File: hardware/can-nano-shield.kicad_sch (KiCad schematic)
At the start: 21 parts, among them J1 Conn_01x15_Socket, J2 Conn_01x15_Socket, J3 Conn_01x04_Pin, J4 Screw_Terminal_01x03, U1 MCP2515-xSO, U2 TJA1051T-3, Y2 16MHz 9pF

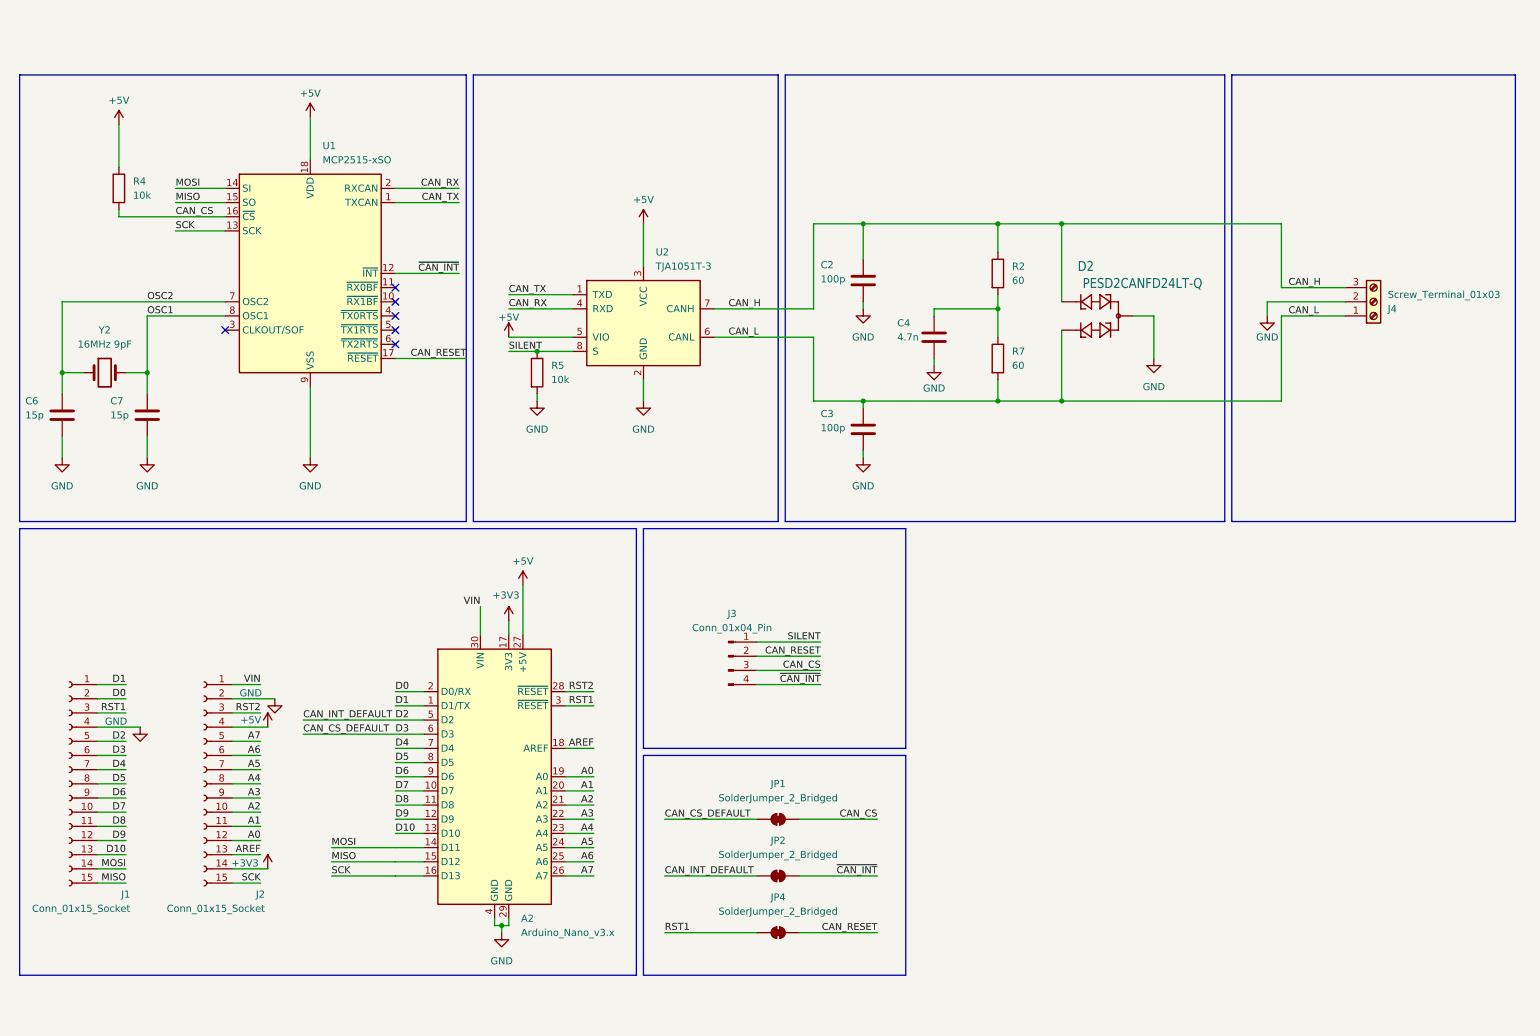
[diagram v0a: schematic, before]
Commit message: added image with cmc revision
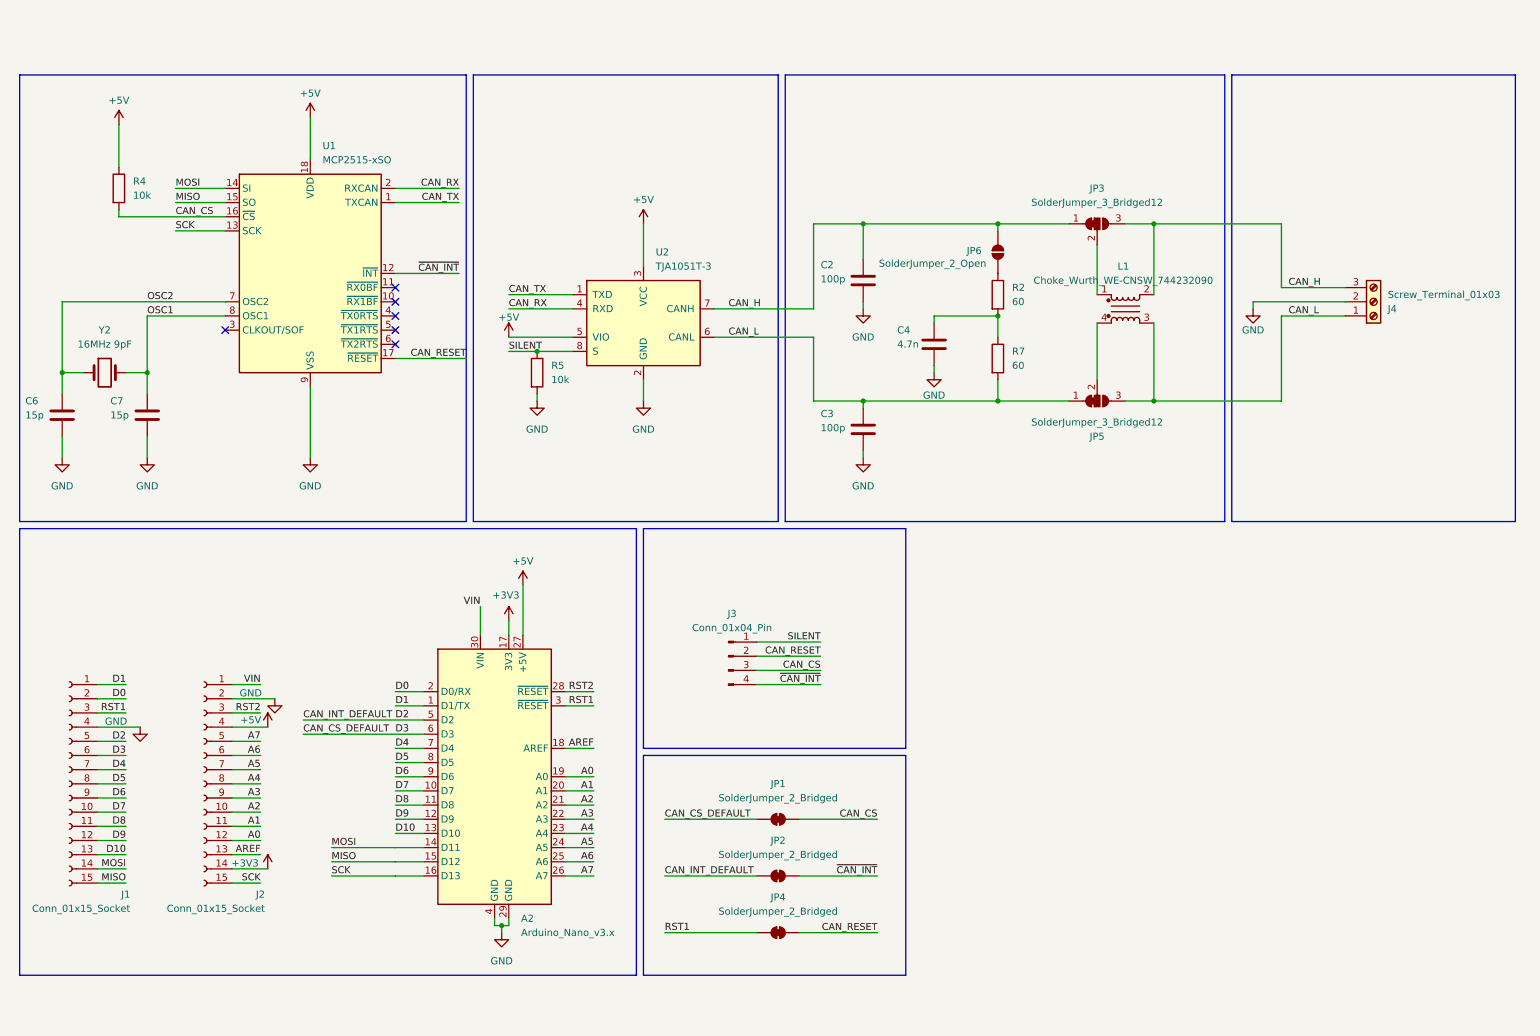
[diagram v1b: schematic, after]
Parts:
- removed D2: PESD2CANFD24LT-Q, Package_TO_SOT_SMD:TSOT-23, symbol kml-custom:PESD2CANFD24LT-Q
- added JP3, JP5: SolderJumper_3_Bridged12, symbol Jumper:SolderJumper_3_Bridged12
- added JP6: SolderJumper_2_Open, symbol Jumper:SolderJumper_2_Open
- added L1: Choke_Wurth_WE-CNSW_744232090, Inductor_SMD:L_CommonMode_Wurth_WE-CNSW-1206, symbol Filter:Choke_Wurth_WE-CNSW_744232090
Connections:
- net CAN_H: now also JP3.1 (A), JP3.3 (B), JP6.1 (A), L1.2; no longer R2.1
- net CAN_L: now also JP5.1 (A), JP5.3 (B), L1.3
- new net: JP6.2 (B), R2.1
- new net: JP5.2 (C), L1.4
- new net: JP3.2 (C), L1.1
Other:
- moved on the sheet: C4, R2

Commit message: updated with cmc inductor + esd diode + emc caps on H L inputs
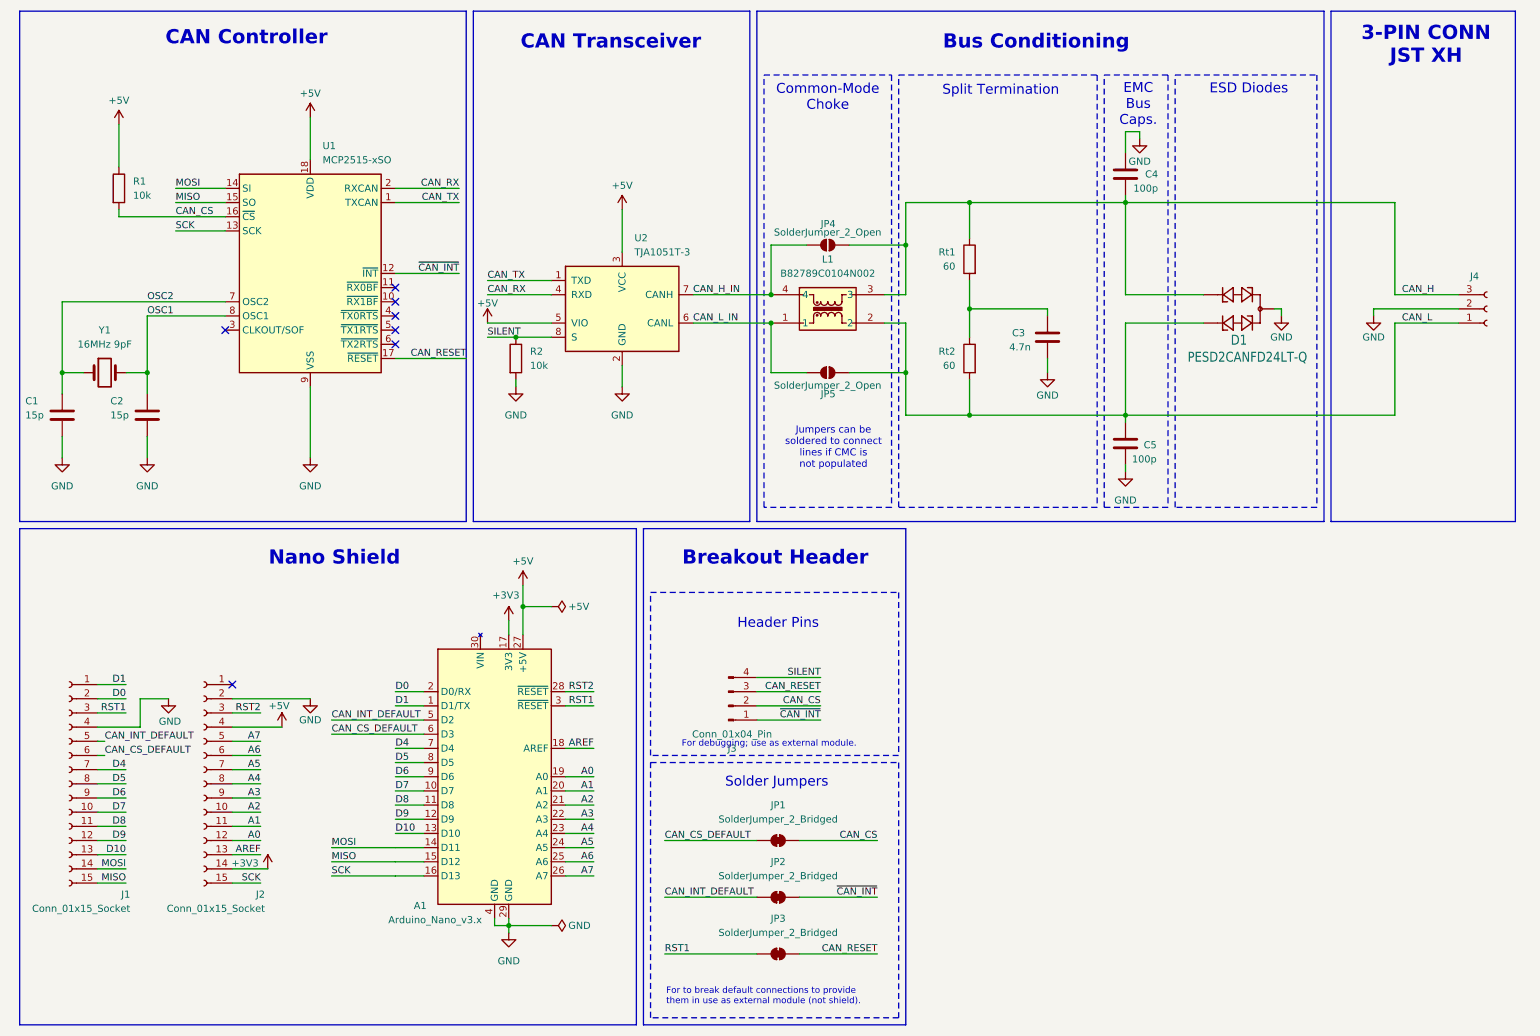
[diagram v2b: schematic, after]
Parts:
- removed J4: Screw_Terminal_01x03, TerminalBlock_4Ucon:TerminalBlock_4Ucon_1x03_P3.50mm_Vertical, symbol Connector:Screw_Terminal_01x03
- removed JP3, JP5: SolderJumper_3_Bridged12, symbol Jumper:SolderJumper_3_Bridged12
- removed JP6: SolderJumper_2_Open, symbol Jumper:SolderJumper_2_Open
- removed L1: Choke_Wurth_WE-CNSW_744232090, Inductor_SMD:L_CommonMode_Wurth_WE-CNSW-1206, symbol Filter:Choke_Wurth_WE-CNSW_744232090
- removed R7: 60, Resistor_SMD:R_0805_2012Metric_Pad1.20x1.40mm_HandSolder, symbol Device:R
- added D1: PESD2CANFD24LT-Q, Package_TO_SOT_SMD:TSOT-23, symbol kml-custom:PESD2CANFD24LT-Q
- added J4: Conn_01x03_Socket, Connector_JST:JST_XH_S3B-XH-A-1_1x03_P2.50mm_Horizontal, symbol Connector:Conn_01x03_Socket
- added JP4, JP5: SolderJumper_2_Open, Jumper:SolderJumper-2_P1.3mm_Open_RoundedPad1.0x1.5mm, symbol Jumper:SolderJumper_2_Open
- added L1: B82789C0104N002, kml-custom:B82789C0113N002, symbol kml-custom:B82789C0104N002
- added Rt2: 60, Resistor_SMD:R_0805_2012Metric_Pad1.20x1.40mm_HandSolder, symbol Device:R
- renumbered A2 to A1, C6 to C1, C7 to C2, C4 to C3, C2 to C4, C3 to C5, JP4 to JP3, R4 to R1, R5 to R2, R2 to Rt1, Y2 to Y1
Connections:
- net CAN_CS: now also J3.2 (Pin_2); no longer J3.3 (Pin_3)
- net CAN_H: now also C4.2, Rt1.1, D1.1, J4.3 (Pin_3), JP4.2 (B), L1.3; no longer C4.1, U2.7 (CANH)
- net CAN_L: now also D1.2, J4.1 (Pin_1), JP5.2 (B), L1.2, Rt2.2; no longer U2.6 (CANL)
- net CAN_RESET: now also J3.3 (Pin_3); no longer J3.2 (Pin_2)
- net GND: now also C4.1, D1.3, J4.2 (Pin_2); no longer C4.2
- net SILENT: now also J3.4 (Pin_4); no longer J3.1 (Pin_1)
- net ~{CAN_INT}: now also J3.1 (Pin_1); no longer J3.4 (Pin_4)
- net at C3.1, Rt1.2: now also Rt2.1
- net VIN: no longer names the net of A1.30 (VIN)
- net VIN: no longer J2.1 (Pin_1)
- new net CAN_H_IN: JP4.1 (A), L1.4, U2.7 (CANH)
- new net CAN_L_IN: JP5.1 (A), L1.1, U2.6 (CANL)
- no-connect marks 6 -> 7
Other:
- note added: "3-PIN CONN JST XH"
- note added: "Breakout Header"
- note added: "Bus Conditioning"
- note added: "CAN Controller"
- note added: "CAN Transceiver"
- note added: "Common-Mode Choke"
- note added: "EMC Bus Caps."
- note added: "ESD Diodes"
- note added: "For debugging; use as external module."
- note added: "For to break default connections to provide them in use as external module (not shield)."
- note added: "Header Pins"
- note added: "Jumpers can be soldered to connect lines if CMC is not populated"
- note added: "Nano Shield"
- note added: "Solder Jumpers"
- note added: "Split Termination"
- moved on the sheet: C3, C4, C5, J3, JP1, JP2, JP3, R2, Rt1, U2

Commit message: added outputs
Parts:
- removed J1, J2: Conn_01x15_Socket, Connector_PinHeader_2.54mm:PinHeader_1x15_P2.54mm_Vertical, symbol Connector:Conn_01x15_Socket
- removed L1: B82789C0104N002, kml-custom:B82789C0113N002, symbol kml-custom:B82789C0104N002
- added J1, J2: SSQ-115-03-T-S, kml-custom:SAMTEC_SSQ-115-03-T-S, symbol kml-custom:SSQ-115-03-T-S
- added T1: B82789C0113N002, kml-custom:SMT_13N002_TDK, symbol kml-custom:B82789C0113N002
- R1: footprint Capacitor_SMD:C_0805_2012Metric_Pad1.18x1.45mm_HandSolder -> Resistor_SMD:R_0805_2012Metric_Pad1.20x1.40mm_HandSolder
- renumbered JP4 to JP1, JP5 to JP2, JP1 to JP3, JP2 to JP4, JP3 to JP5
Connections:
- net +3V3: now also J2.14
- net +5V: now also J2.04
- net A0: now also J2.12
- net A1: now also J2.11
- net A2: now also J2.10
- net A3: now also J2.09
- net A4: now also J2.08
- net A5: now also J2.07
- net A6: now also J2.06
- net A7: now also J2.05
- net AREF: now also J2.13
- net CAN_CS_DEFAULT: now also J1.06
- net CAN_H: now also J4.1 (Pin_1), T1.2; no longer J4.3 (Pin_3)
- net CAN_H_IN: now also T1.1
- net CAN_INT_DEFAULT: now also J1.05
- net CAN_L: now also J4.3 (Pin_3), T1.3; no longer J4.1 (Pin_1)
- net CAN_L_IN: now also T1.4
- net D0: now also J1.02
- net D1: now also J1.01
- net D10: now also J1.13
- net D4: now also J1.07
- net D5: now also J1.08
- net D6: now also J1.09
- net D7: now also J1.10
- net D8: now also J1.11
- net D9: now also J1.12
- net GND: now also J1.04, J2.02
- net MISO: now also J1.15
- net MOSI: now also J1.14
- net RST1: now also J1.03
- net RST2: now also J2.03
- net SCK: now also J2.15
- net VIN: now reaches A1.30 (VIN)
- net VIN: now also J2.01
- no-connect marks 7 -> 6
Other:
- note added: "D2"
- note added: "D3"
- moved on the sheet: C3, J3, JP1, JP2, JP3, JP4, JP5, Rt1, Rt2
